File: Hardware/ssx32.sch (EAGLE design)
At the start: 81 parts, among them IC1 PIC18F45K20, IC2 FT232RL, IC3 TXB0108PW, IC4 TXB0108PW, IC5 TXB0108PW, IC6 TXB0108PW, IC7 78L33, IC8 74AHC1G32DBV, X1 8, X10 1, X11 19, X12 16, X13 15, X14 14, X15 13, X16 12, X17 11, X18 10, X19 9, X20 20, X21 21, X22 22, X23 23, X24 24, X25 25, X26 26, X27 27, X28 28, X29 29, X3 17, X30 30, X31 31, X32 32, X33 1751248, X34 18, X35 USB, X4 7, X5 6, X6 5, X7 4, X8 3, X9 2

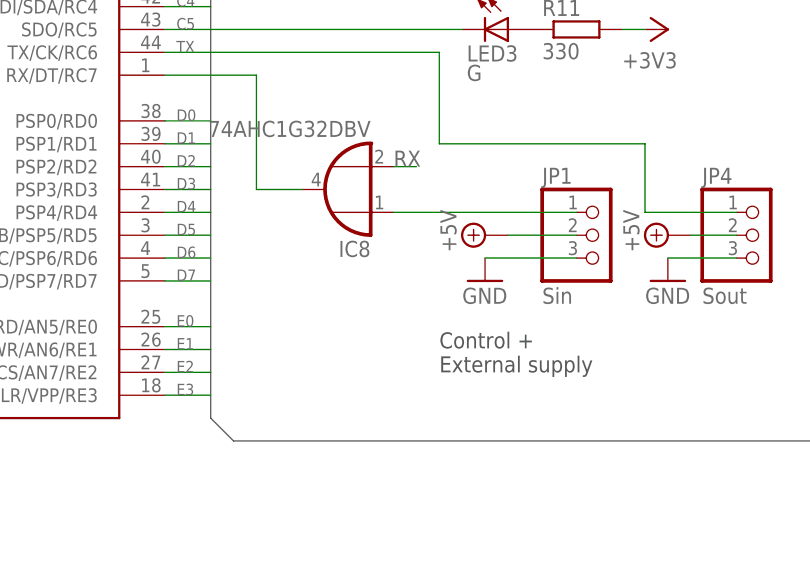
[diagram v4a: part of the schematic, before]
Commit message: Added software, minor board changes
Added software
Added resistor for not mounted ftdi chip
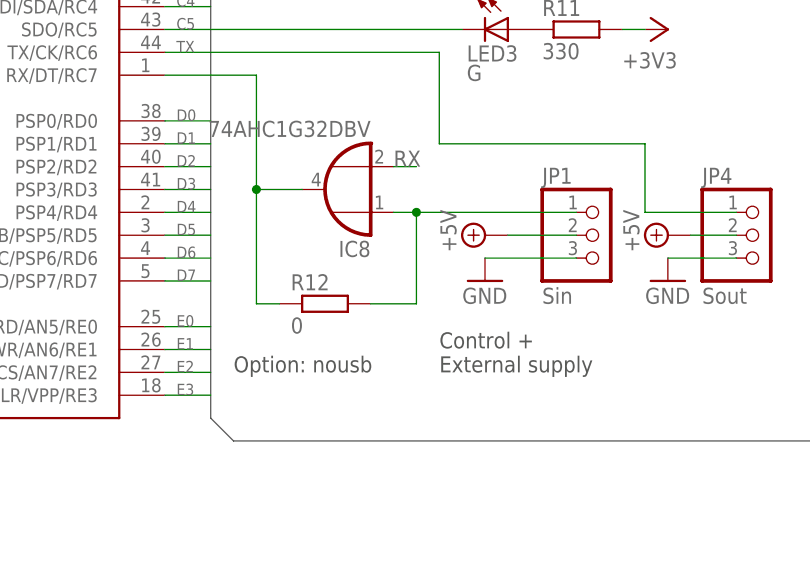
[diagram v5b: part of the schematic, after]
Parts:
- added R12: 0, rcl:R-EU_R0603
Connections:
- net N$48: now also R12.1
- net N$54: now also R12.2
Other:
- note added: "Option: nousb"
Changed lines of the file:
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@@
 <part name="LED4" library="led" deviceset="LED" device="CHIPLED_0603" value="G"/>
 <part name="R10" library="rcl" deviceset="R-EU_" device="R0603" value="330"/>
+<part name="R12" library="rcl" deviceset="R-EU_" device="R0603" value="0"/>
 </parts>
 <sheets>
@@
 <text x="172.72" y="50.8" size="1.778" layer="97">Control +
 External supply</text>
+<text x="149.86" y="50.8" size="1.778" layer="97">Option: nousb</text>
 </plain>
 <instances>
@@
 <instance part="LED4" gate="G$1" x="73.66" y="215.9"/>
 <instance part="R10" gate="G$1" x="73.66" y="223.52" rot="R90"/>
+<instance part="R12" gate="G$1" x="160.02" y="58.42"/>
 </instances>
 <busses>
@@
 <pinref part="JP1" gate="A" pin="1"/>
 <pinref part="IC8" gate="A" pin="I0"/>
-<wire x1="167.64" y1="68.58" x2="187.96" y2="68.58" width="0.1524" layer="91"/>
+<wire x1="167.64" y1="68.58" x2="170.18" y2="68.58" width="0.1524" layer="91"/>
+<pinref part="R12" gate="G$1" pin="2"/>
+<wire x1="170.18" y1="68.58" x2="187.96" y2="68.58" width="0.1524" layer="91"/>
+<wire x1="165.1" y1="58.42" x2="170.18" y2="58.42" width="0.1524" layer="91"/>
+<wire x1="170.18" y1="58.42" x2="170.18" y2="68.58" width="0.1524" layer="91"/>
+<junction x="170.18" y="68.58"/>
 </segment>
 </net>
@@
 <pinref part="IC1" gate="G$2" pin="RX/DT/RC7"/>
 <wire x1="152.4" y1="83.82" x2="142.24" y2="83.82" width="0.1524" layer="91"/>
-</segment>
-</net>
+<pinref part="R12" gate="G$1" pin="1"/>
+<wire x1="154.94" y1="58.42" x2="152.4" y2="58.42" width="0.1524" layer="91"/>
+<wire x1="152.4" y1="58.42" x2="152.4" y2="71.12" width="0.1524" layer="91"/>
+<junction x="152.4" y="71.12"/>
+</segment>
+</net>

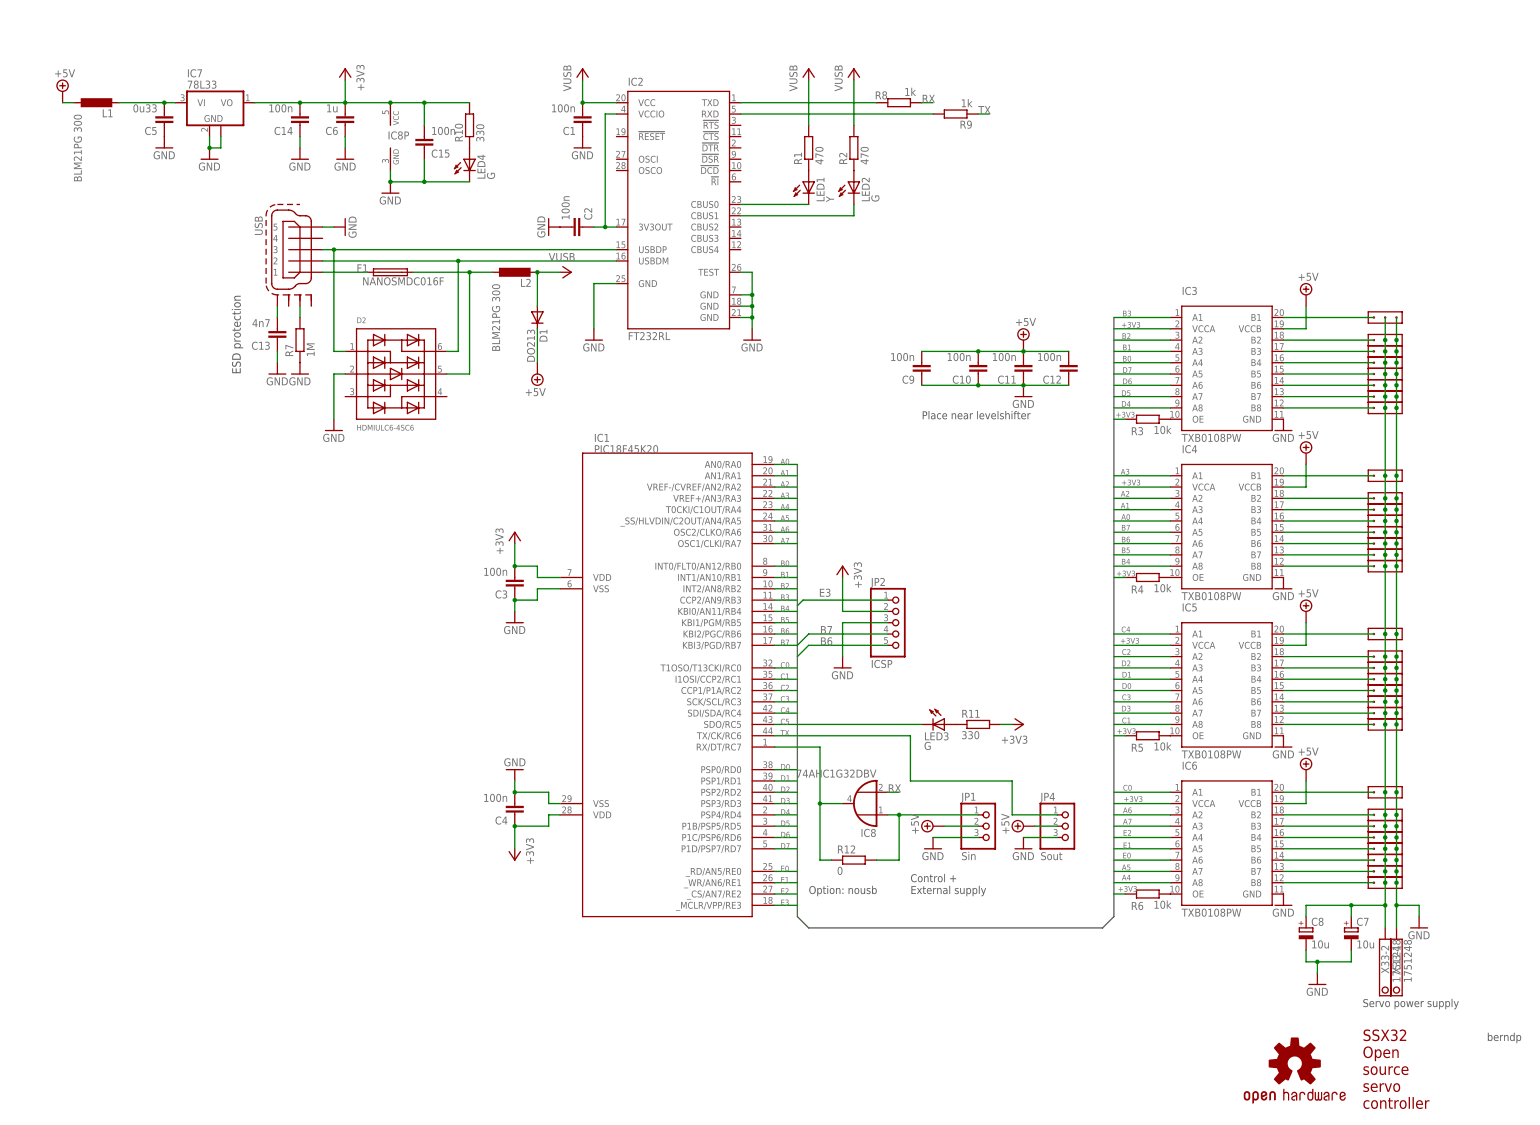
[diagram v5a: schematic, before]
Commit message: Revert "Revert "Fixed schematic errors""
This reverts commit 02a030f20bdd3dfa1fc93a39d84e363c4da10222.
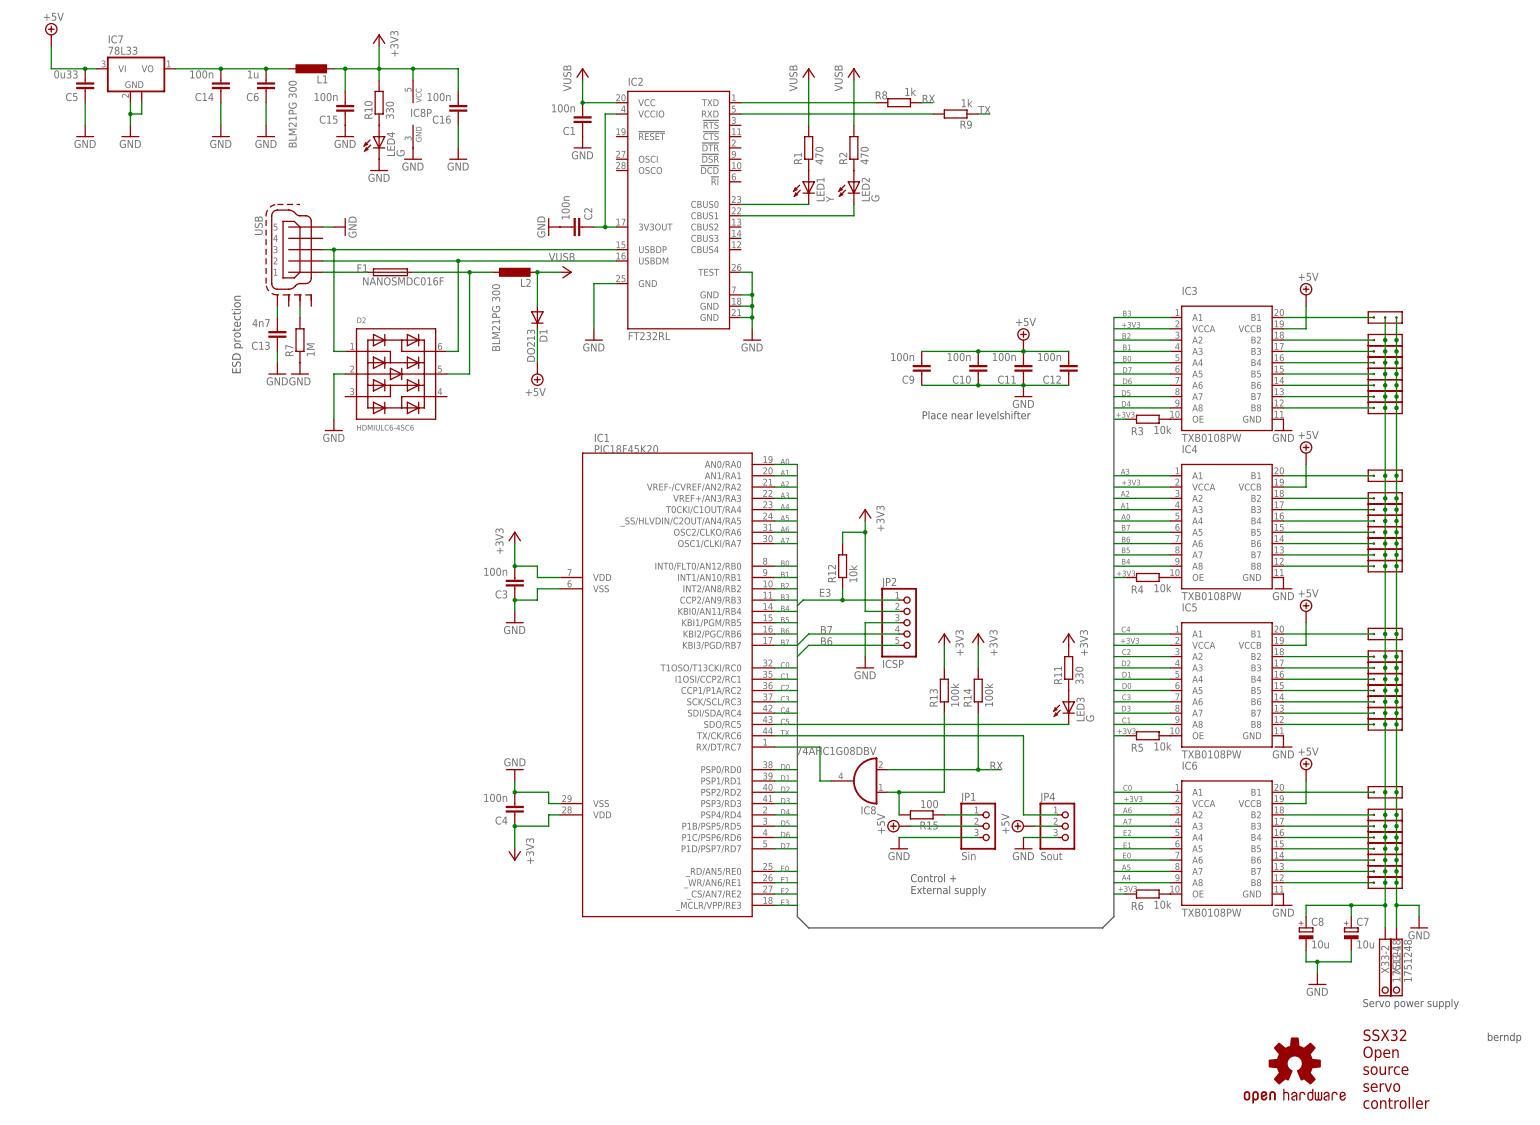
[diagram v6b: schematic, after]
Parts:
- added C16: 100n, rcl:C-EUC0603
- added R13, R14: 100k, rcl:R-EU_R0603
- added R15: 100, rcl:R-EU_R0603
- IC8: value 74AHC1G32DBV -> 74AHC1G08DBV; device 74xx-little-de:74AHC1G32DBV -> 74xx-little-de:74AHC1G08DBV
- R12: value 0 -> 10k
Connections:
- removed net N$54: IC8A.I0, JP1.1, R12.2
- new net N$42: IC1.RX/DT/RC7, IC8A.O
- new net N$7: C14.2, C6.2, IC7.VO, L1.1
- net +3V3: now also C16.2, L1.2, R12.2, R13.2, R14.2; no longer C14.2, C6.2, IC7.VO
- net +UB: now also C5.2, IC7.VI; no longer L1.1
- net E3: now also R12.1
- net GND: now also C16.1
- net N$46: now also IC8A.I0, R13.1, R15.2; no longer C5.2, IC7.VI, L1.2
- net N$48: now also JP1.1, R15.1; no longer IC1.RX/DT/RC7, IC8A.O, R12.1
- net RX: now also R14.1
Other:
- note removed: "Option: nousb"
- moved on the sheet: C14, C15, C5, C6, IC7, IC8P, JP2, L1, LED3, LED4, R10, R11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

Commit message: Revert "Fixed schematic errors"
This reverts commit bc55cbd2c08a143a3db725eeb6975bb6eadbf5e7.
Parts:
- removed C16: 100n, rcl:C-EUC0603
- removed R13, R14: 100k, rcl:R-EU_R0603
- removed R15: 100, rcl:R-EU_R0603
- IC8: value 74AHC1G08DBV -> 74AHC1G32DBV; device 74xx-little-de:74AHC1G08DBV -> 74xx-little-de:74AHC1G32DBV
- R12: value 10k -> 0
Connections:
- removed net N$42: IC1.RX/DT/RC7, IC8A.O
- removed net N$7: C14.2, C6.2, IC7.VO, L1.1
- new net N$54: IC8A.I0, JP1.1, R12.2
- net +3V3: now also C14.2, C6.2, IC7.VO; no longer C16.2, L1.2, R12.2, R13.2, R14.2
- net +UB: now also L1.1; no longer C5.2, IC7.VI
- net E3: no longer R12.1
- net GND: no longer C16.1
- net N$46: now also C5.2, IC7.VI, L1.2; no longer IC8A.I0, R13.1, R15.2
- net N$48: now also IC1.RX/DT/RC7, IC8A.O, R12.1; no longer JP1.1, R15.1
- net RX: no longer R14.1
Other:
- note added: "Option: nousb"
- moved on the sheet: C14, C15, C5, C6, IC7, IC8P, JP2, L1, LED3, LED4, R10, R11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

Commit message: Revert "Added software, minor board changes"
This reverts commit cd959f70c37cd81d74ff6deb02d888d0a529ccba.
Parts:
- removed R12: 0, rcl:R-EU_R0603
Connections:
- net N$48: no longer R12.1
- net N$54: no longer R12.2
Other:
- note removed: "Option: nousb"
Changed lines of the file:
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@@
 <part name="LED4" library="led" deviceset="LED" device="CHIPLED_0603" value="G"/>
 <part name="R10" library="rcl" deviceset="R-EU_" device="R0603" value="330"/>
-<part name="R12" library="rcl" deviceset="R-EU_" device="R0603" value="0"/>
 </parts>
 <sheets>
@@
 <text x="172.72" y="50.8" size="1.778" layer="97">Control +
 External supply</text>
-<text x="149.86" y="50.8" size="1.778" layer="97">Option: nousb</text>
 </plain>
 <instances>
@@
 <instance part="LED4" gate="G$1" x="73.66" y="215.9"/>
 <instance part="R10" gate="G$1" x="73.66" y="223.52" rot="R90"/>
-<instance part="R12" gate="G$1" x="160.02" y="58.42"/>
 </instances>
 <busses>
@@
 <pinref part="JP1" gate="A" pin="1"/>
 <pinref part="IC8" gate="A" pin="I0"/>
-<wire x1="167.64" y1="68.58" x2="170.18" y2="68.58" width="0.1524" layer="91"/>
-<pinref part="R12" gate="G$1" pin="2"/>
-<wire x1="170.18" y1="68.58" x2="187.96" y2="68.58" width="0.1524" layer="91"/>
-<wire x1="165.1" y1="58.42" x2="170.18" y2="58.42" width="0.1524" layer="91"/>
-<wire x1="170.18" y1="58.42" x2="170.18" y2="68.58" width="0.1524" layer="91"/>
-<junction x="170.18" y="68.58"/>
+<wire x1="167.64" y1="68.58" x2="187.96" y2="68.58" width="0.1524" layer="91"/>
 </segment>
 </net>
@@
 <pinref part="IC1" gate="G$2" pin="RX/DT/RC7"/>
 <wire x1="152.4" y1="83.82" x2="142.24" y2="83.82" width="0.1524" layer="91"/>
-<pinref part="R12" gate="G$1" pin="1"/>
-<wire x1="154.94" y1="58.42" x2="152.4" y2="58.42" width="0.1524" layer="91"/>
-<wire x1="152.4" y1="58.42" x2="152.4" y2="71.12" width="0.1524" layer="91"/>
-<junction x="152.4" y="71.12"/>
-</segment>
-</net>
+</segment>
+</net>
